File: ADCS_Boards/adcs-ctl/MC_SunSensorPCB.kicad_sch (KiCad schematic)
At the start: 120 parts, among them J1 PC104_Connector, J2 PPTC062LJBN-RC, J3 Conn_01x03_Female, Q12 20V/0.2A/8MHz/1.2Ω/1Vth, Q14 20V/0.2A/8MHz/1.2Ω/1Vth, Q3 20V/0.2A/8MHz/1.2Ω/1Vth, Q4 20V/0.2A/8MHz/1.2Ω/1Vth, Q6 20V/0.2A/8MHz/1.2Ω/1Vth, Q9 20V/0.2A/8MHz/1.2Ω/1Vth, U1 9DoF IMU, U10 Op-Amp, U11 Op-Amp, U12 Op-Amp, U13 Op-Amp, U14 1.8V/100mA, U15 STM32F103RET6, U16 MR25H10MDF, U17 1825232-1, U2 1.8V/100mA, U3 9DoF IMU, U4 DF13-7P-1.25DS(20), U5 DF13-7P-1.25DS(20), U6 DF13-7P-1.25DS(20), U7 DF13-7P-1.25DS(20), U8 LM358, U9 CD74HC4067M96, Y1 Crystal_GND24

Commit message: adcs: udpated rwl-db and adcs-ctl on behalf of Yasin
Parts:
- removed D2: RED, SparkFun_IMU_Breakout_ICM-20948:LED-0603, symbol SparkFun_IMU_Breakout_ICM-20948-eagle-import:LED-RED0603
- removed JP5: I2C PU, SparkFun_IMU_Breakout_ICM-20948:SMT-JUMPER_3_2-NC_TRACE_SILK, symbol SparkFun_IMU_Breakout_ICM-20948-eagle-import:JUMPER-SMT_3_2-NC_TRACE_SILK
- removed JP6: LED, SparkFun_IMU_Breakout_ICM-20948:SMT-JUMPER_2_NC_TRACE_SILK, symbol SparkFun_IMU_Breakout_ICM-20948-eagle-import:JUMPER-SMT_2_NC_TRACE_SILK
- removed Q12, Q14, Q6, Q9: 20V/0.2A/8MHz/1.2Ω/1Vth, SparkFun_IMU_Breakout_ICM-20948:SOT-416FL, symbol SparkFun_IMU_Breakout_ICM-20948-eagle-import:MOSFET-NCH-RE1C002UN
- removed R1, R3, R32, R33, R40, R43, R46, R47: 2.2k, SparkFun_IMU_Breakout_ICM-20948:0402-TIGHT, symbol SparkFun_IMU_Breakout_ICM-20948-eagle-import:2.2KOHM-0402T-1/16W-1%
- removed R51: 220, SparkFun_IMU_Breakout_ICM-20948:0603, symbol SparkFun_IMU_Breakout_ICM-20948-eagle-import:220OHM-0603-1/10W-1%
- removed TP2: 1.8V, SparkFun_IMU_Breakout_ICM-20948:PAD.03X.03, symbol SparkFun_IMU_Breakout_ICM-20948-eagle-import:TEST-POINT3
- removed U2: 1.8V/100mA, SparkFun_IMU_Breakout_ICM-20948:SC70, symbol SparkFun_IMU_Breakout_ICM-20948-eagle-import:V_REG_SP6214-1.8V
- J2: footprint Footprints_QSAT:PPTC062LJBN-RC -> Connector_PinHeader_2.54mm:PinHeader_2x06_P2.54mm_Horizontal
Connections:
- net +5V: no longer C30.1
- net 1.8V: now also C30.1, U3.9 (AD0/SDO)
- net GND: now also U1.9 (AD0/SDO); no longer Y1.2, Y1.4
- net IMU_SCL: no longer Q4.2 (S), R28.1
- net IMU_SDA: no longer Q3.2 (S), R26.1
- net RCC_OSC_IN: now also Y1.2, Y1.4; no longer Y1.1
- net AD0/SDO renamed PB2
- net PB2: no longer U3.9 (AD0/SDO)
- net AD0/SDO_2 renamed PB5
- net PB5: no longer U1.9 (AD0/SDO)
- new net SCL/SCLK: Q4.2 (S), R28.1
- new net SDA/SDI: Q3.2 (S), R26.1
- no-connect marks 76 -> 77
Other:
- moved on the sheet: TP1

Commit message: Board updated
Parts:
- removed JP2: I2C PU, SparkFun_IMU_Breakout_ICM-20948:SMT-JUMPER_3_2-NC_TRACE_SILK, symbol SparkFun_IMU_Breakout_ICM-20948-eagle-import:JUMPER-SMT_3_2-NC_TRACE_SILK
- removed JP3: LED, SparkFun_IMU_Breakout_ICM-20948:SMT-JUMPER_2_NC_TRACE_SILK, symbol SparkFun_IMU_Breakout_ICM-20948-eagle-import:JUMPER-SMT_2_NC_TRACE_SILK
- added C42, C43: 10uF, SparkFun_IMU_Breakout_ICM-20948:0603, symbol SparkFun_IMU_Breakout_ICM-20948-eagle-import:1.0UF-0603-16V-10%-X7R
- added TP2: 3V3, SparkFun_IMU_Breakout_ICM-20948:PAD.03X.03, symbol SparkFun_IMU_Breakout_ICM-20948-eagle-import:TEST-POINT3
- added U2: BU33SA5WGWZ-E2, Footprints_QSAT:BU33SA5WGWZ-E2, symbol qsat5to3.3-rescue:BU33SA5WGWZ-E2-qsat-symb
- J2: footprint Connector_PinHeader_2.54mm:PinHeader_2x06_P2.54mm_Horizontal -> Connector_PinSocket_2.54mm:PinSocket_2x06_P2.54mm_Horizontal
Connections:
- net SCL/SCLK_VIN is gone; now on net IMU_SCL: Q4.3 (D), R29.1
- net SDA/SDI_VIN is gone; now on net IMU_SDA: Q3.3 (D), R27.1
- net +3V3: now also R27.2, R29.2, C43.2, TP2.P$1 (1), U2.2 (Output); no longer J1.79 (H2-27)
- net +5V: now also C42.1, U2.3 (Input)
- net GND: now also R36.1, C42.2, C43.1, U2.1 (GND)
- net IMU_SCL: no longer U1.23 (SCL/SCLK), U3.23 (SCL/SCLK)
- net IMU_SDA: no longer U1.24 (SDA/SDI), U3.24 (SDA/SDI)
- net SCL/SCLK renamed SCL/SCLK
- net SCL/SCLK: now also U1.23 (SCL/SCLK), U3.23 (SCL/SCLK)
- net SDA/SDI renamed SDA/SDI
- net SDA/SDI: now also U1.24 (SDA/SDI), U3.24 (SDA/SDI)
- no-connect marks 77 -> 78
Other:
- note added: "1v8 Power Generation"
- note added: "3v3 Power Generation"
- note added: "Crystal Oscillator"
- note added: "I2C Pullups"
- note added: "IMU Circuitry"
- note added: "MRAM Persistant Storage"
- note added: "PMOD"
- note added: "SWD"
- note added: "Sun Sensor Circuitry"
- note removed: "Cut to disable PWR LED"
- note removed: "VIN 1.8V to 5.5V"
- moved on the sheet: C1, C10, C11, C12, C13, C14, C15, C16, C17, C18, C19, C2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

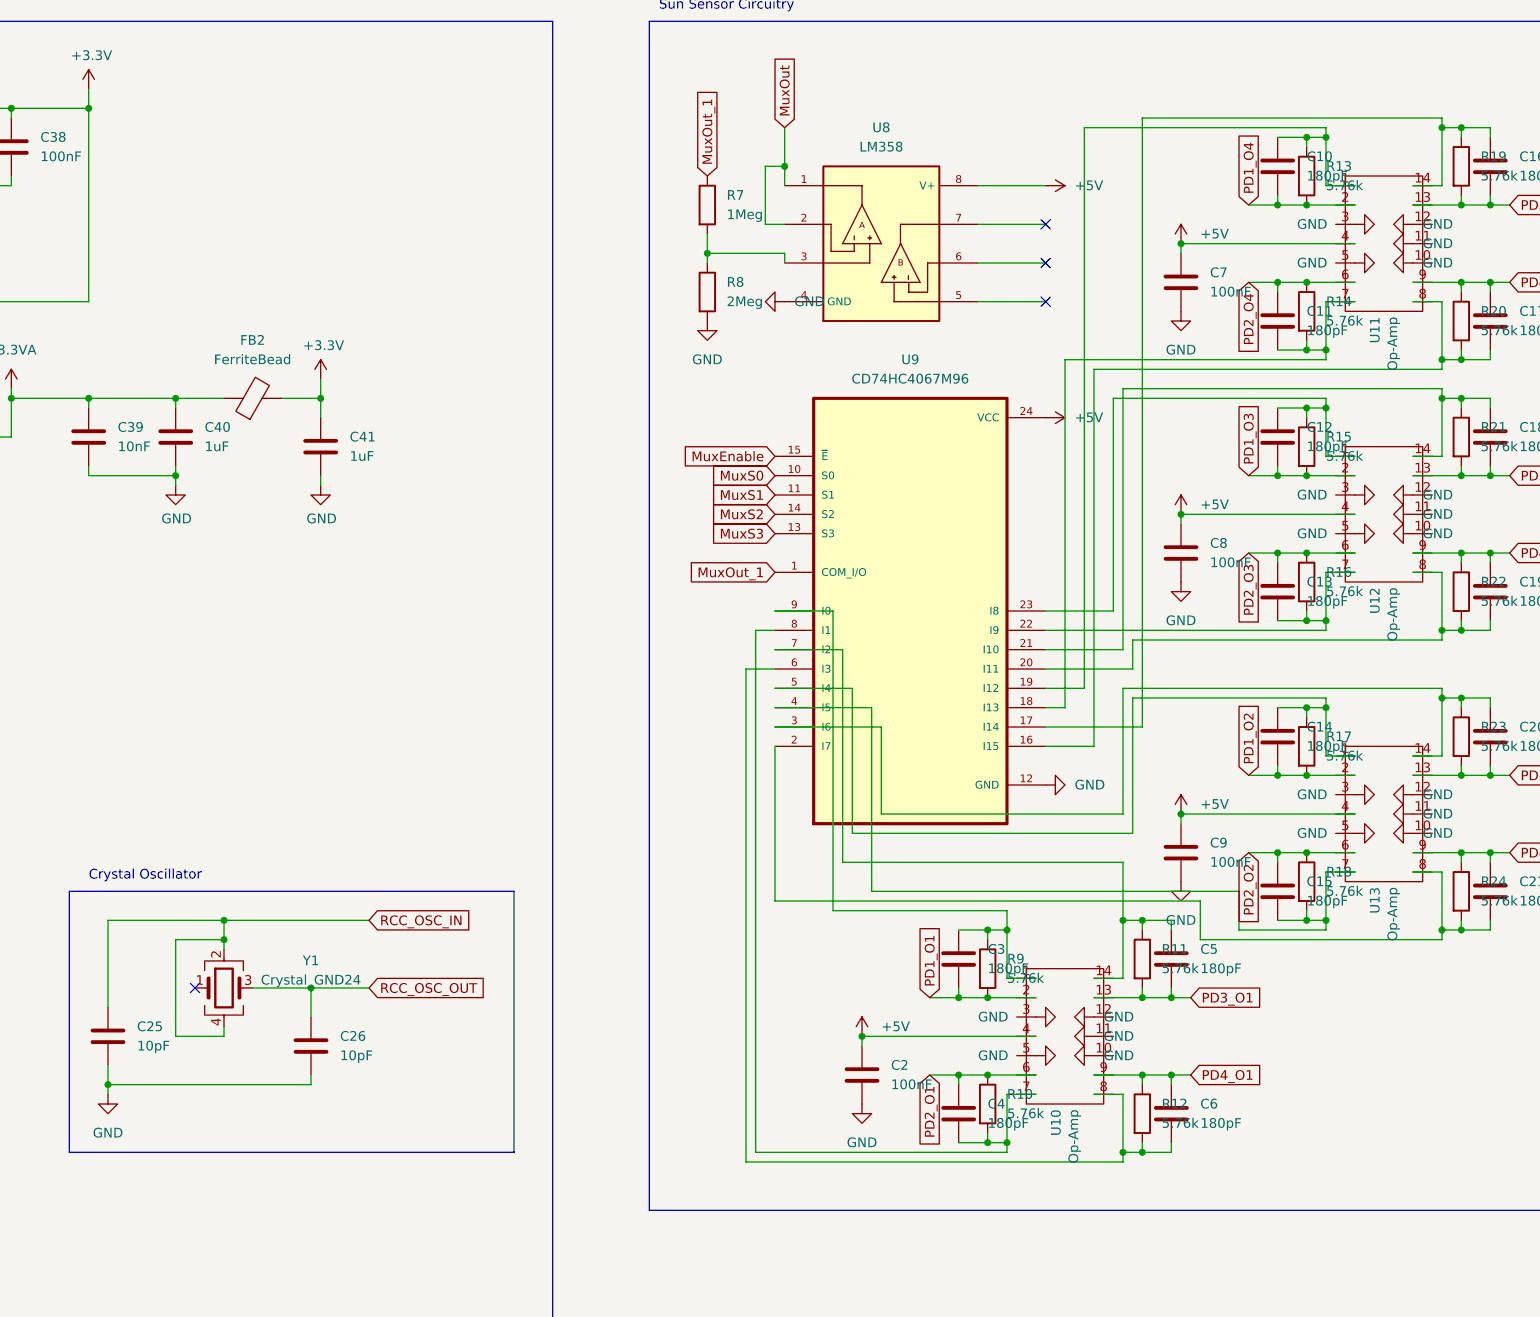
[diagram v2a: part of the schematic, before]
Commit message: adcs: adcs-ctl: continued silkscreen changes
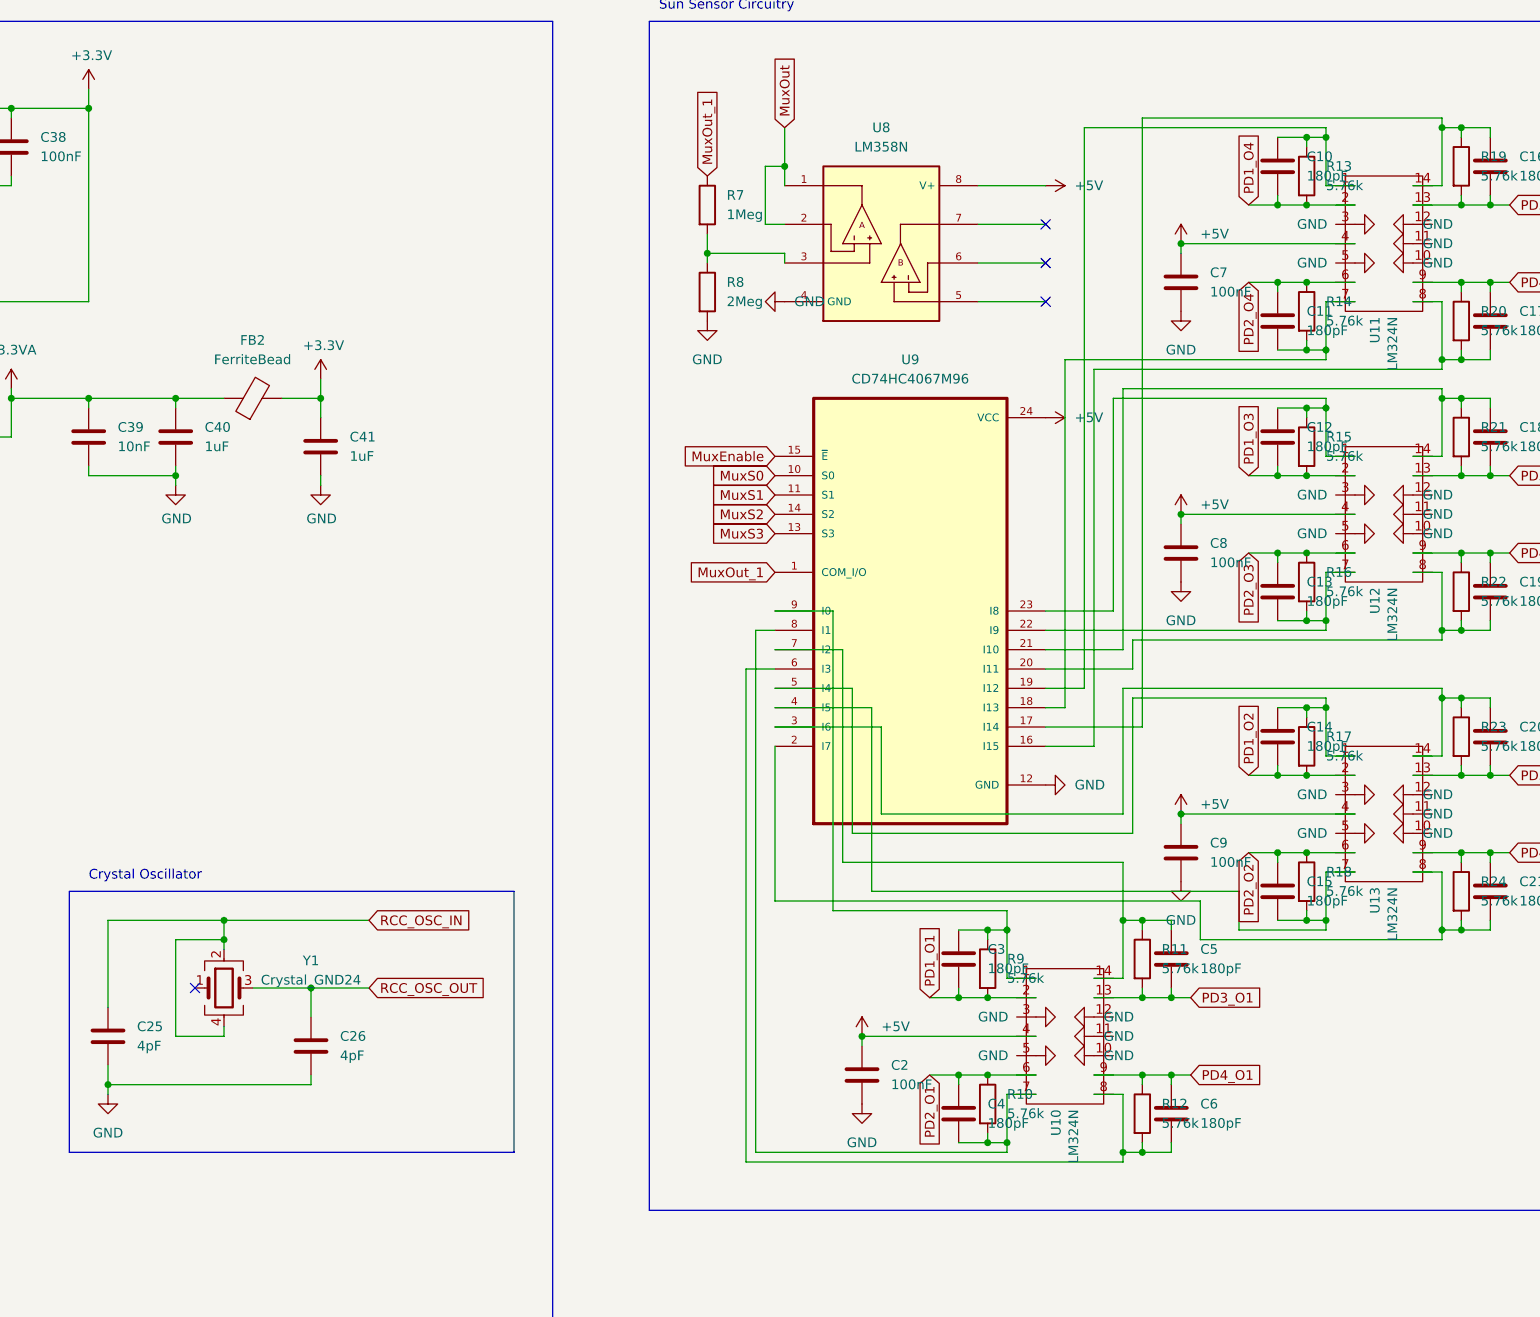
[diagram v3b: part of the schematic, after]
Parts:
- C25, C26: value 10pF -> 4pF
- U10, U11, U12, U13: value Op-Amp -> LM324N
- U8: value LM358 -> LM358N
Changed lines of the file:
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@@
       (effects (font (size 1.27 1.27)) (justify left))
     )
-    (property "Value" "10pF" (id 1) (at 275.59 232.4099 0)
+    (property "Value" "4pF" (id 1) (at 275.59 232.4099 0)
       (effects (font (size 1.27 1.27)) (justify left))
     )
@@
       (effects (font (size 1.27 1.27)) (justify left))
     )
-    (property "Value" "10pF" (id 1) (at 302.26 233.6799 0)
+    (property "Value" "4pF" (id 1) (at 302.26 233.6799 0)
       (effects (font (size 1.27 1.27)) (justify left))
     )
@@
       (effects (font (size 1.27 1.27)) (justify left))
     )
-    (property "Value" "Op-Amp" (id 1) (at 398.653 240.7412 0)
+    (property "Value" "LM324N" (id 1) (at 398.653 240.7412 0)
       (effects (font (size 1.27 1.27)) (justify left))
     )
@@
       (effects (font (size 1.27 1.27)) (justify left))
     )
-    (property "Value" "Op-Amp" (id 1) (at 440.563 211.5312 0)
+    (property "Value" "LM324N" (id 1) (at 440.563 211.5312 0)
       (effects (font (size 1.27 1.27)) (justify left))
     )
@@
       (effects (font (size 1.27 1.27)) (justify left))
     )
-    (property "Value" "Op-Amp" (id 1) (at 440.563 172.1612 0)
+    (property "Value" "LM324N" (id 1) (at 440.563 172.1612 0)
       (effects (font (size 1.27 1.27)) (justify left))
     )
@@
     (in_bom yes) (on_board yes) (fields_autoplaced)
     (property "Reference" "U8" (id 0) (at 373.38 111.76 0))
-    (property "Value" "LM358" (id 1) (at 373.38 114.3 0))
+    (property "Value" "LM358N" (id 1) (at 373.38 114.3 0))
     (property "Footprint" "Footprints_QSAT:DIP794W45P254L959H508Q8" (id 2) (at 373.38 138.43 0)
       (effects (font (size 1.27 1.27)) hide)
@@
   (symbol (lib_id "power:+3V3") (at 209.55 306.07 0) (unit 1)
     (in_bom yes) (on_board yes) (fields_autoplaced)
-    (property "Reference" "#PWR?" (id 0) (at 209.55 309.88 0)
+    (property "Reference" "#PWR0123" (id 0) (at 209.55 309.88 0)
       (effects (font (size 1.27 1.27)) hide)
     )
@@
       (effects (font (size 1.27 1.27)) (justify left))
     )
-    (property "Value" "Op-Amp" (id 1) (at 440.563 136.6012 0)
+    (property "Value" "LM324N" (id 1) (at 440.563 136.6012 0)
       (effects (font (size 1.27 1.27)) (justify left))
     )
@@
       (reference "#PWR0122") (unit 1) (value "GND") (footprint "")
     )
+    (path "/9fa69c05-e98e-4d06-96e4-a355a7534015"
+      (reference "#PWR0123") (unit 1) (value "+3V3") (footprint "")
+    )
     (path "/fe8bdc46-9b36-4523-a214-d22228987e65"
       (reference "#PWR0124") (unit 1) (value "+5V") (footprint "")
@@
       (reference "#PWR0185") (unit 1) (value "+3V3") (footprint "")
     )
-    (path "/9fa69c05-e98e-4d06-96e4-a355a7534015"
-      (reference "#PWR?") (unit 1) (value "+3V3") (footprint "")
-    )
     (path "/bbf90661-060b-49a9-92a0-bd0459e0c08e"
       (reference "#SUPPLY0101") (unit 1) (value "1.8V") (footprint "SparkFun_IMU_Breakout_ICM-20948:")
@@
     )
     (path "/3ce11e1c-c74d-4a14-b5c6-dd616f9deb94"
-      (reference "C25") (unit 1) (value "10pF") (footprint "Capacitor_SMD:C_0603_1608Metric")
+      (reference "C25") (unit 1) (value "4pF") (footprint "Capacitor_SMD:C_0603_1608Metric")
     )
     (path "/48f19526-49fa-4e38-9d97-f7970fd92371"
-      (reference "C26") (unit 1) (value "10pF") (footprint "Capacitor_SMD:C_0603_1608Metric")
+      (reference "C26") (unit 1) (value "4pF") (footprint "Capacitor_SMD:C_0603_1608Metric")
     )
     (path "/d155c323-e8f1-4066-8048-874dc289a330"
@@
     )
     (path "/8c1ad99d-77f7-4b10-b696-4684887a8fe2"
-      (reference "U8") (unit 1) (value "LM358") (footprint "Footprints_QSAT:DIP794W45P254L959H508Q8")
+      (reference "U8") (unit 1) (value "LM358N") (footprint "Footprints_QSAT:DIP794W45P254L959H508Q8")
     )
     (path "/06f5e4be-dd56-4051-996e-05a0d498a116"
@@
     )
     (path "/4fa61966-363c-4f7f-98b7-e175cf401f1c"
-      (reference "U10") (unit 1) (value "Op-Amp") (footprint "Footprints_QSAT:Op-Amp")
+      (reference "U10") (unit 1) (value "LM324N") (footprint "Footprints_QSAT:Op-Amp")
     )
     (path "/c8663ff2-7e7c-45a8-b968-53676533f774"
-      (reference "U11") (unit 1) (value "Op-Amp") (footprint "Footprints_QSAT:Op-Amp")
+      (reference "U11") (unit 1) (value "LM324N") (footprint "Footprints_QSAT:Op-Amp")
     )
     (path "/5900f713-0160-4ed8-91c1-7af29c40d854"
-      (reference "U12") (unit 1) (value "Op-Amp") (footprint "Footprints_QSAT:Op-Amp")
+      (reference "U12") (unit 1) (value "LM324N") (footprint "Footprints_QSAT:Op-Amp")
     )
     (path "/5509793f-eaba-434a-8b6d-15d70ad11efc"
-      (reference "U13") (unit 1) (value "Op-Amp") (footprint "Footprints_QSAT:Op-Amp")
+      (reference "U13") (unit 1) (value "LM324N") (footprint "Footprints_QSAT:Op-Amp")
     )
     (path "/fad3c9ff-04d9-4979-95c0-84d47f0aa4bb"
